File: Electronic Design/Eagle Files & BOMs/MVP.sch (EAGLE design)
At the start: 35 parts, among them IC1 ACS712ELC-5A, IC2 ATMEGA328-PU, Q1 IRF9540, Q2 IRF9540, X1 16MHz

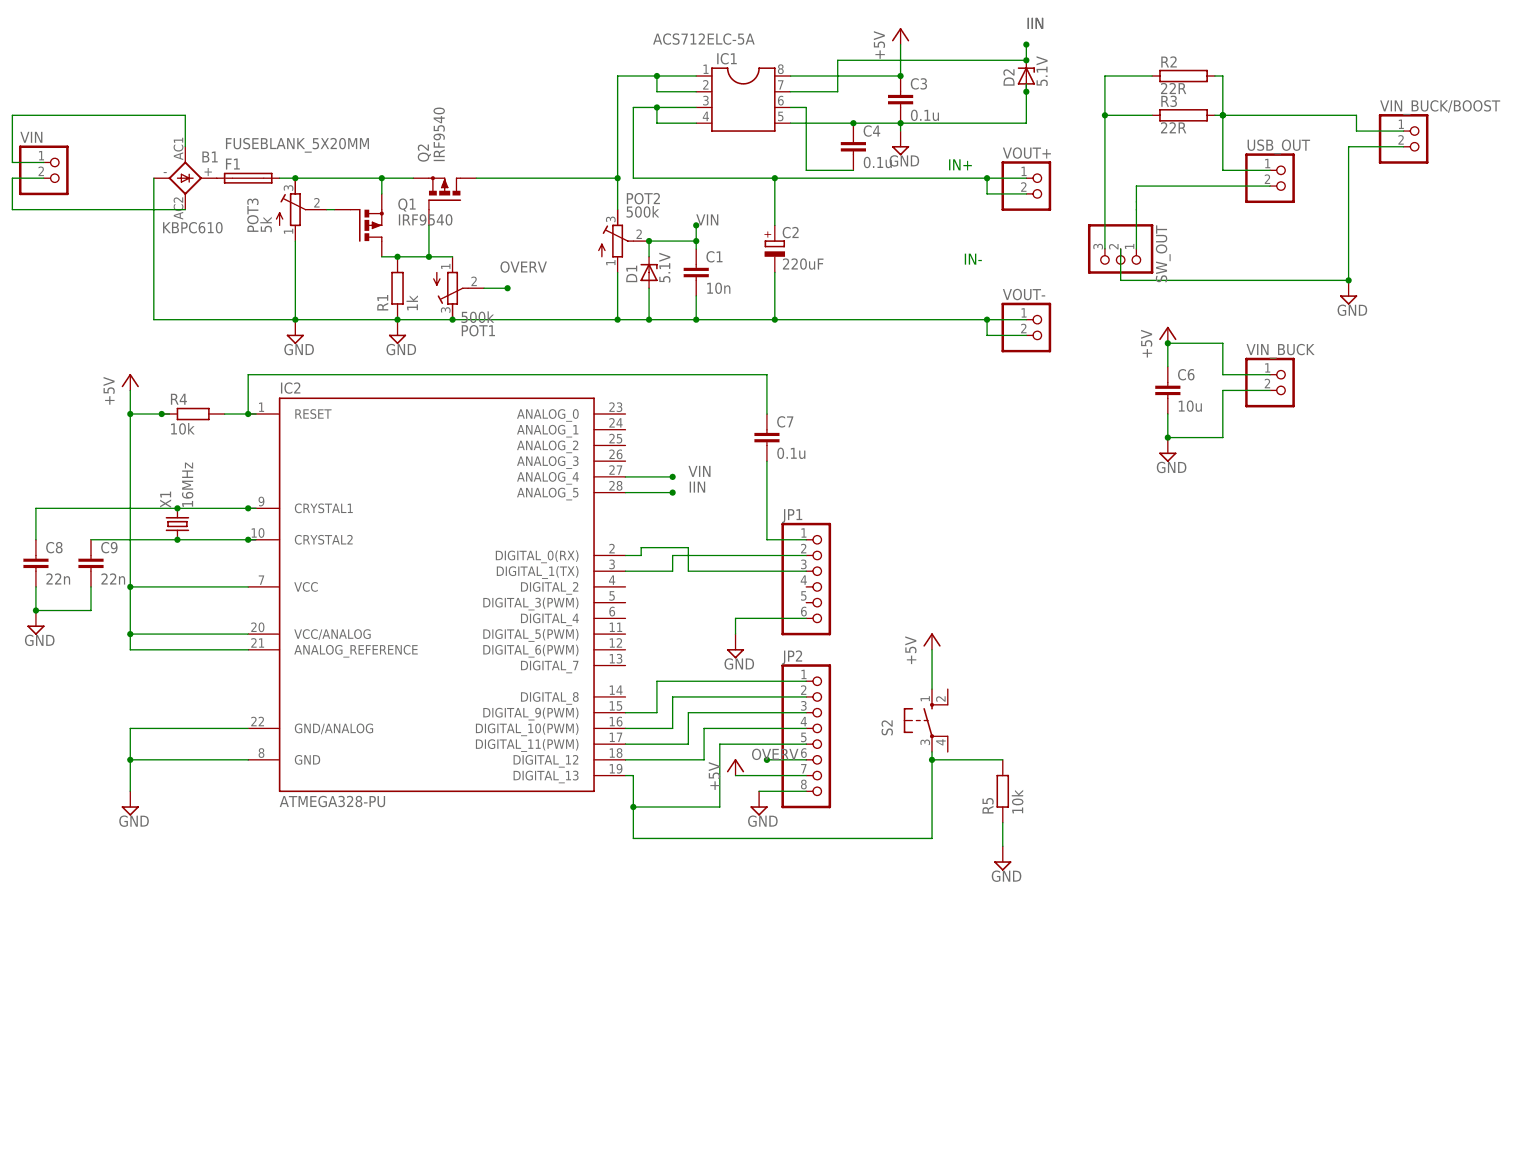
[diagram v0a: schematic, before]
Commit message: updating folder structure and improving naming in MVP board
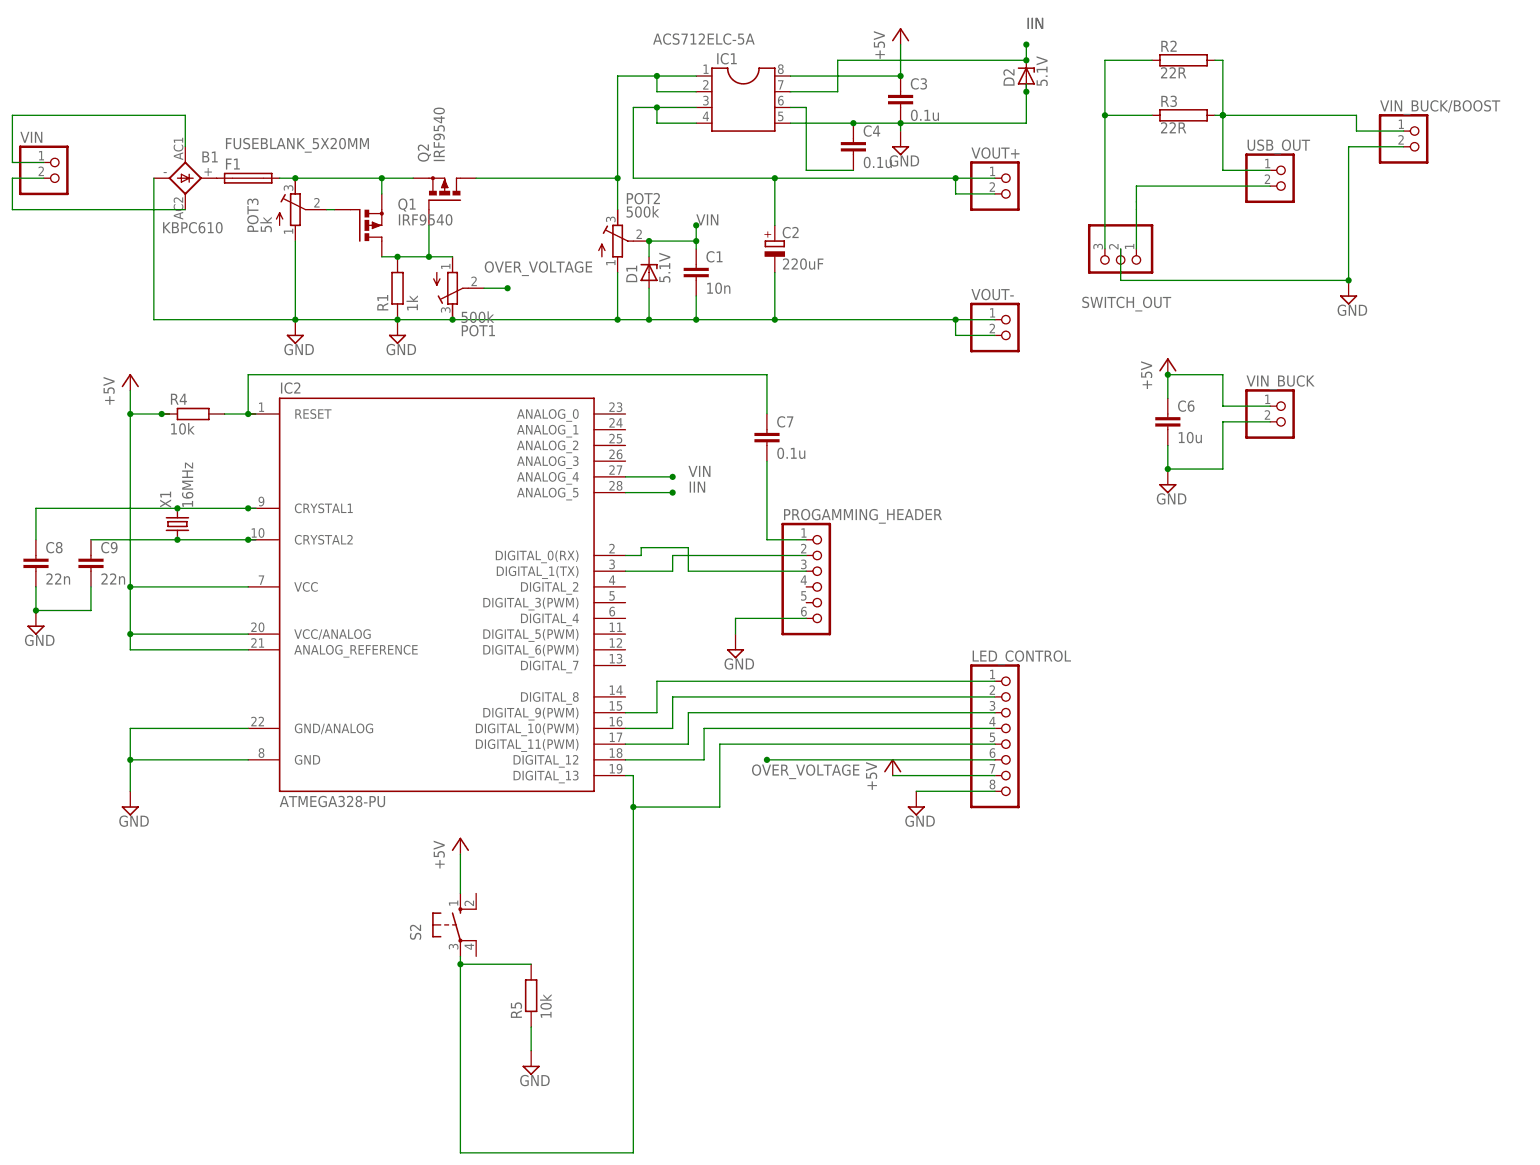
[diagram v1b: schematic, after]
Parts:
- removed JP2: (no value), pinhead:PINHD-1X8
- added LED_CONTROL: (no value), pinhead:PINHD-1X8
- renumbered JP1 to PROGAMMING_HEADER, SW_OUT to SWITCH_OUT
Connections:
- removed net OVERV: JP2.6, POT1.S
- new net OVER_VOLTAGE: LED_CONTROL.6, POT1.S
- net +5V: now also LED_CONTROL.7; no longer JP2.7
- net GND: now also LED_CONTROL.8; no longer JP2.8
- net N$11: now also LED_CONTROL.3; no longer JP2.3
- net N$12: now also LED_CONTROL.4; no longer JP2.4
- net N$6: now also LED_CONTROL.1; no longer JP2.1
- net N$8: now also LED_CONTROL.5; no longer JP2.5
- net N$9: now also LED_CONTROL.2; no longer JP2.2
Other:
- note removed: "IN+"
- note removed: "IN-"
- moved on the sheet: C6, R2, R5, S2, VIN_BUCK, VOUT+, VOUT-

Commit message: changed that name of header to LED_CONTROL_IN / OUT
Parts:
- renumbered LED_CONTROL to LED_CONTROL_OUT
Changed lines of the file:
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@@
 <part name="SUPPLY14" library="supply2" deviceset="GND" device=""/>
 <part name="SUPPLY17" library="supply2" deviceset="GND" device=""/>
-<part name="LED_CONTROL" library="pinhead" deviceset="PINHD-1X8" device=""/>
+<part name="LED_CONTROL_OUT" library="pinhead" deviceset="PINHD-1X8" device=""/>
 <part name="VOUT-" library="pinhead" deviceset="PINHD-1X2" device=""/>
 <part name="VIN_BUCK" library="pinhead" deviceset="PINHD-1X2" device=""/>
@@
 <instance part="SUPPLY14" gate="GND" x="-107.95" y="16.51"/>
 <instance part="SUPPLY17" gate="GND" x="34.29" y="-12.7"/>
-<instance part="LED_CONTROL" gate="A" x="49.53" y="-2.54"/>
+<instance part="LED_CONTROL_OUT" gate="A" x="49.53" y="-2.54"/>
 <instance part="VOUT-" gate="G$1" x="49.53" y="63.5"/>
 <instance part="VIN_BUCK" gate="G$1" x="93.98" y="49.53"/>
@@
 </segment>
 <segment>
-<pinref part="LED_CONTROL" gate="A" pin="8"/>
+<pinref part="LED_CONTROL_OUT" gate="A" pin="8"/>
 <pinref part="SUPPLY17" gate="GND" pin="GND"/>
 <wire x1="46.99" y1="-10.16" x2="34.29" y2="-10.16" width="0.1524" layer="91"/>
@@
 <segment>
 <pinref part="+5V3" gate="1" pin="+5V"/>
-<pinref part="LED_CONTROL" gate="A" pin="7"/>
+<pinref part="LED_CONTROL_OUT" gate="A" pin="7"/>
 <wire x1="30.48" y1="-7.62" x2="46.99" y2="-7.62" width="0.1524" layer="91"/>
 </segment>
@@
 <wire x1="2.54" y1="-12.7" x2="-11.43" y2="-12.7" width="0.1524" layer="91"/>
 <junction x="-11.43" y="-12.7"/>
-<pinref part="LED_CONTROL" gate="A" pin="5"/>
+<pinref part="LED_CONTROL_OUT" gate="A" pin="5"/>
 <wire x1="46.99" y1="-2.54" x2="2.54" y2="-2.54" width="0.1524" layer="91"/>
 </segment>
@@
 <wire x1="-12.7" y1="2.54" x2="-7.62" y2="2.54" width="0.1524" layer="91"/>
 <wire x1="-7.62" y1="2.54" x2="-7.62" y2="7.62" width="0.1524" layer="91"/>
-<pinref part="LED_CONTROL" gate="A" pin="1"/>
+<pinref part="LED_CONTROL_OUT" gate="A" pin="1"/>
 <wire x1="-7.62" y1="7.62" x2="46.99" y2="7.62" width="0.1524" layer="91"/>
 </segment>
@@
 <net name="N$9" class="0">
 <segment>
-<pinref part="LED_CONTROL" gate="A" pin="2"/>
+<pinref part="LED_CONTROL_OUT" gate="A" pin="2"/>
 <wire x1="46.99" y1="5.08" x2="-5.08" y2="5.08" width="0.1524" layer="91"/>
 <wire x1="-5.08" y1="5.08" x2="-5.08" y2="0" width="0.1524" layer="91"/>
@@
 <wire x1="-12.7" y1="-2.54" x2="-2.54" y2="-2.54" width="0.1524" layer="91"/>
 <wire x1="-2.54" y1="-2.54" x2="-2.54" y2="2.54" width="0.1524" layer="91"/>
-<pinref part="LED_CONTROL" gate="A" pin="3"/>
+<pinref part="LED_CONTROL_OUT" gate="A" pin="3"/>
 <wire x1="-2.54" y1="2.54" x2="46.99" y2="2.54" width="0.1524" layer="91"/>
 </segment>
@@
 <wire x1="0" y1="-5.08" x2="0" y2="0" width="0.1524" layer="91"/>
 <wire x1="0" y1="0" x2="46.99" y2="0" width="0.1524" layer="91"/>
-<pinref part="LED_CONTROL" gate="A" pin="4"/>
+<pinref part="LED_CONTROL_OUT" gate="A" pin="4"/>
 </segment>
 </net>
@@
 <net name="OVER_VOLTAGE" class="0">
 <segment>
-<pinref part="LED_CONTROL" gate="A" pin="6"/>
+<pinref part="LED_CONTROL_OUT" gate="A" pin="6"/>
 <wire x1="46.99" y1="-5.08" x2="10.16" y2="-5.08" width="0.1524" layer="91"/>
 <junction x="10.16" y="-5.08"/>
